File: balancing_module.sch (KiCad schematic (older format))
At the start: 54 parts

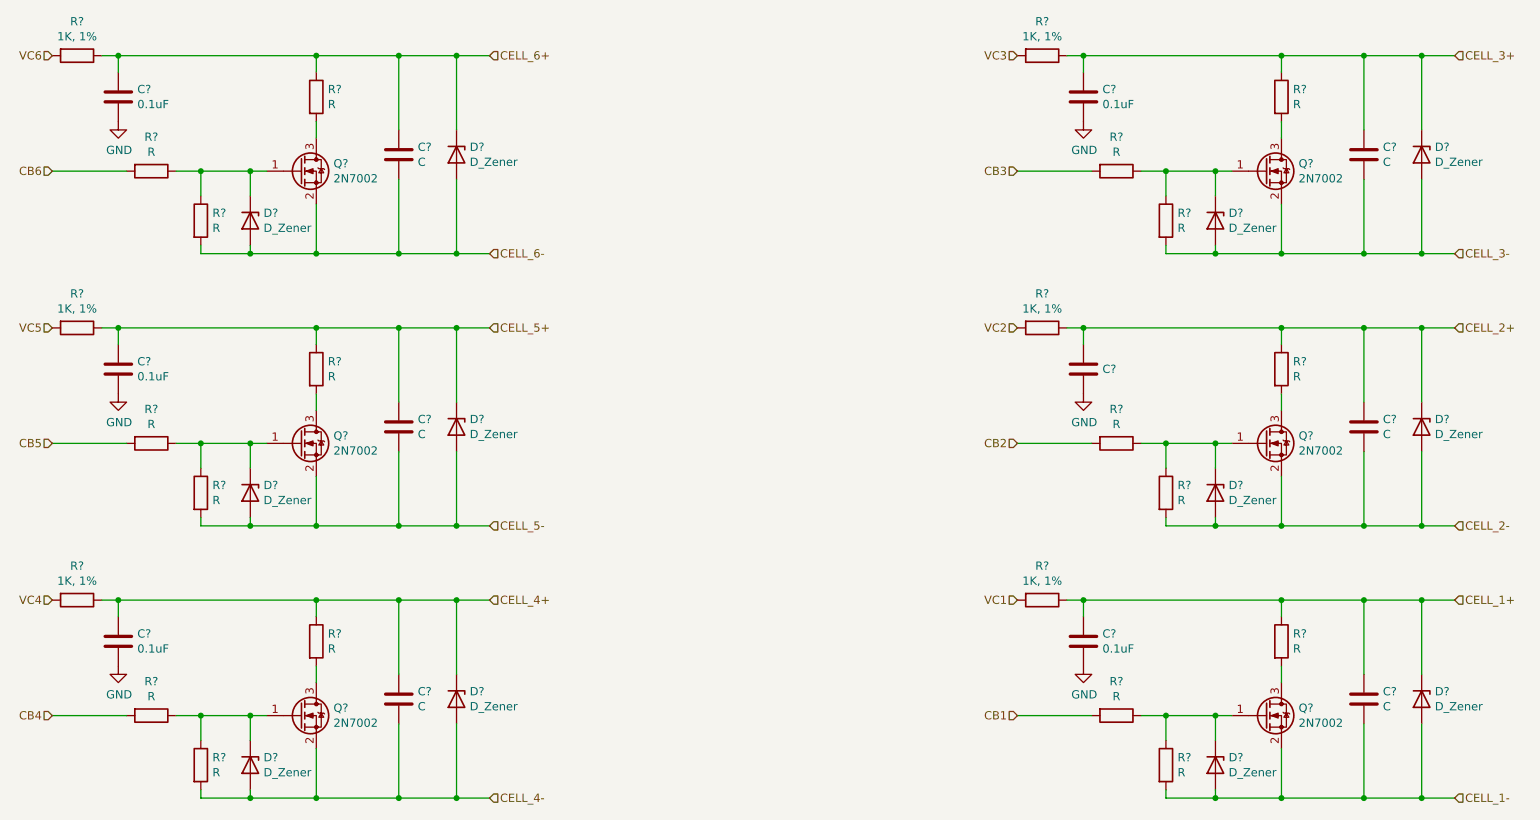
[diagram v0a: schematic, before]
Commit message: mmoya/bq76pl536a Adds current sensor and IO for hierarchical sheet
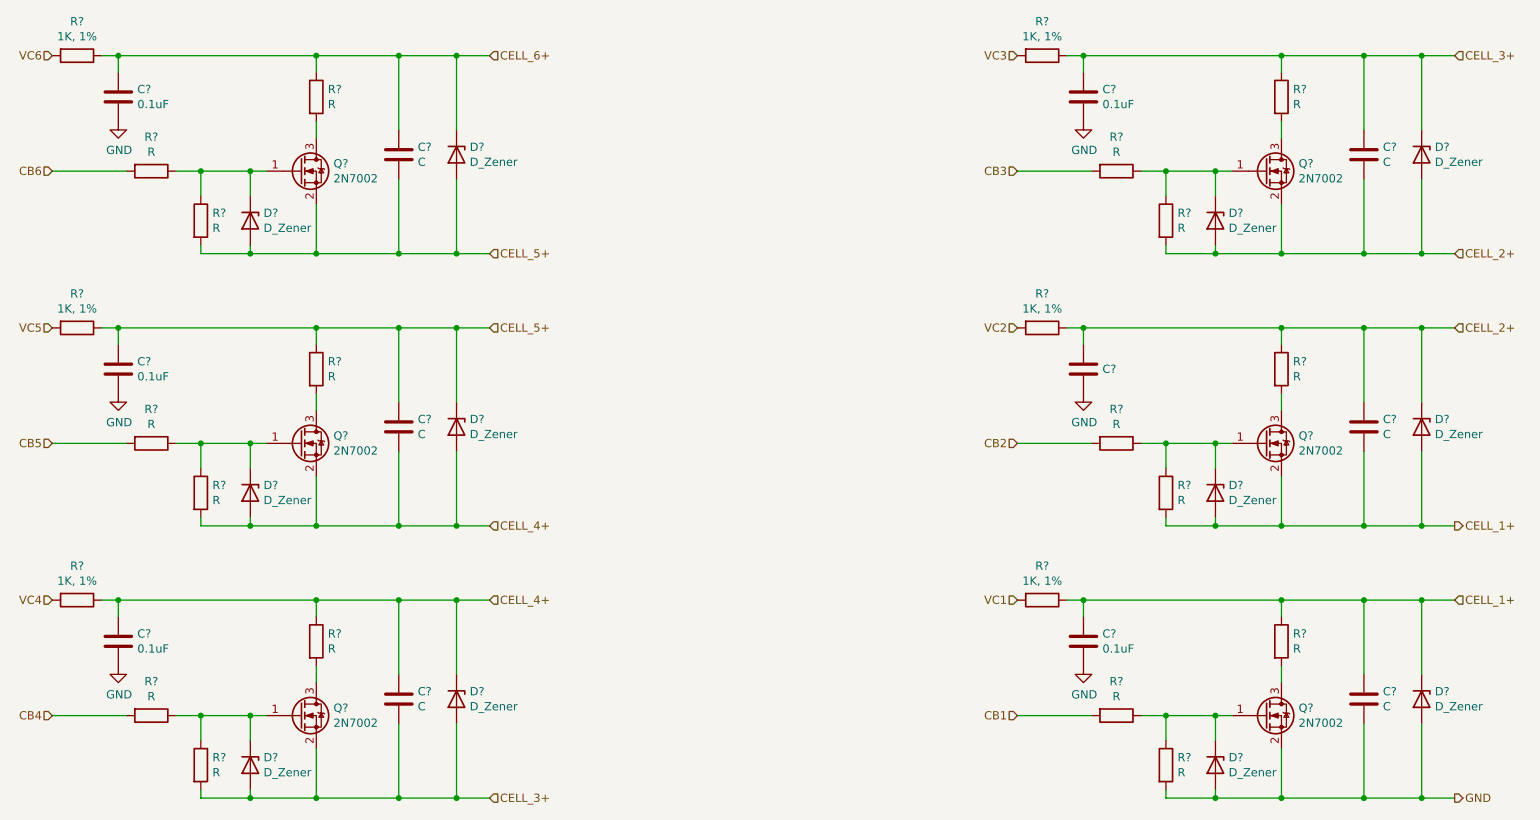
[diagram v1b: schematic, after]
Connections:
- net CELL_1- is gone; now on net GND: C?.2, D?.2 (A), D?.2 (A), Q?.2 (S), R?.2
- net CELL_2- is gone; now on net CELL_1+: C?.2, D?.2 (A), D?.2 (A), Q?.2 (S), R?.2
- net CELL_3- is gone; now on net CELL_2+: C?.2, D?.2 (A), D?.2 (A), Q?.2 (S), R?.2
- net CELL_4- is gone; now on net CELL_3+: C?.2, D?.2 (A), D?.2 (A), Q?.2 (S), R?.2
- net CELL_5- is gone; now on net CELL_4+: C?.2, D?.2 (A), D?.2 (A), Q?.2 (S), R?.2
- net CELL_6- is gone; now on net CELL_5+: C?.2, D?.2 (A), D?.2 (A), Q?.2 (S), R?.2
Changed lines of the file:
@@
 Connection ~ 3900 2300
 Text HLabel 4100 2300 2    50   Input ~ 0
-CELL_6-
+CELL_5+
 $Comp
 L Transistor_FET:2N7002 Q?
@@
 Connection ~ 3900 3950
 Text HLabel 4100 3950 2    50   Input ~ 0
-CELL_5-
+CELL_4+
 $Comp
 L Transistor_FET:2N7002 Q?
@@
 Connection ~ 3900 5600
 Text HLabel 4100 5600 2    50   Input ~ 0
-CELL_4-
+CELL_3+
 $Comp
 L Transistor_FET:2N7002 Q?
@@
 Connection ~ 9750 2300
 Text HLabel 9950 2300 2    50   Input ~ 0
-CELL_3-
+CELL_2+
 $Comp
 L Transistor_FET:2N7002 Q?
@@
 	9950 3950 9750 3950
 Connection ~ 9750 3950
-Text HLabel 9950 3950 2    50   Input ~ 0
-CELL_2-
 $Comp
 L Transistor_FET:2N7002 Q?
@@
 	9950 5600 9750 5600
 Connection ~ 9750 5600
-Text HLabel 9950 5600 2    50   Input ~ 0
-CELL_1-
 Text HLabel 1450 1100 0    50   Input ~ 0
 VC6
 Text HLabel 1450 1800 0    50   Input ~ 0
 CB6
+Text HLabel 9950 5600 2    50   Output ~ 0
+GND
+Text HLabel 9950 3950 2    50   Output ~ 0
+CELL_1+
 $EndSCHEMATC

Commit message: Adds missing footprints for conns
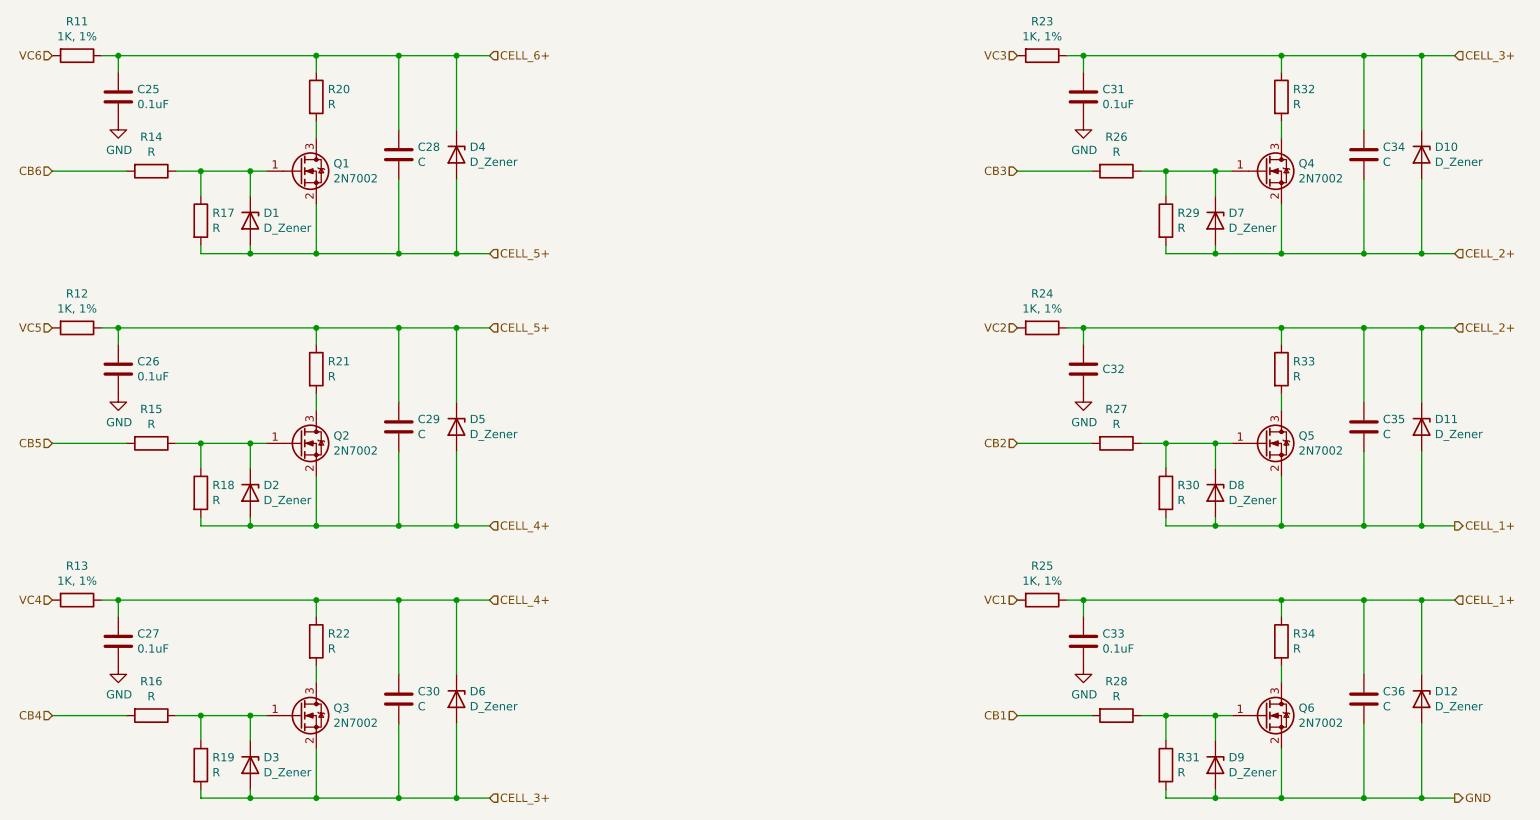
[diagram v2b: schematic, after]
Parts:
- gave numbers to parts that had none: 54
